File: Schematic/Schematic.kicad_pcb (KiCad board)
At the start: 2 copper layers, 1 part, among them U1 STM32F091RCT6

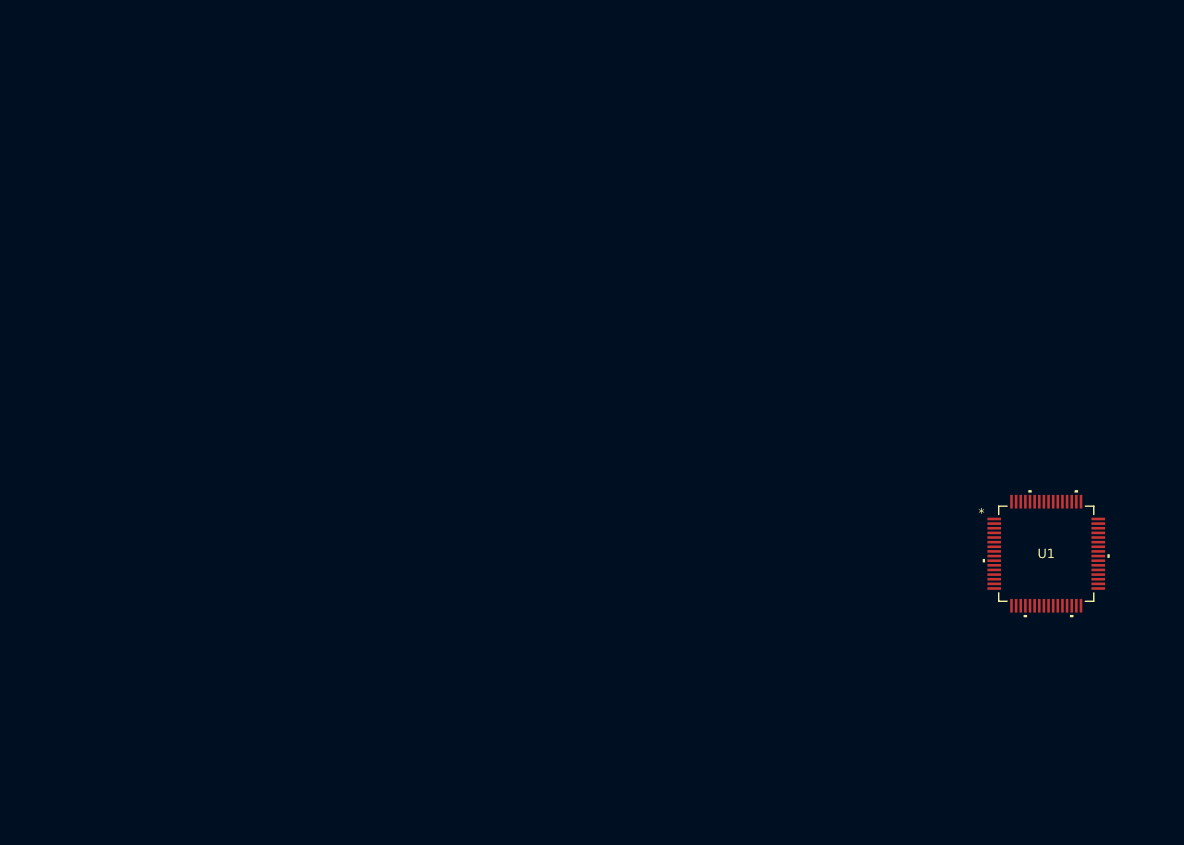
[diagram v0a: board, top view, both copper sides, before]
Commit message: Added paritial schematic including microprocessor, hub75 and keypad
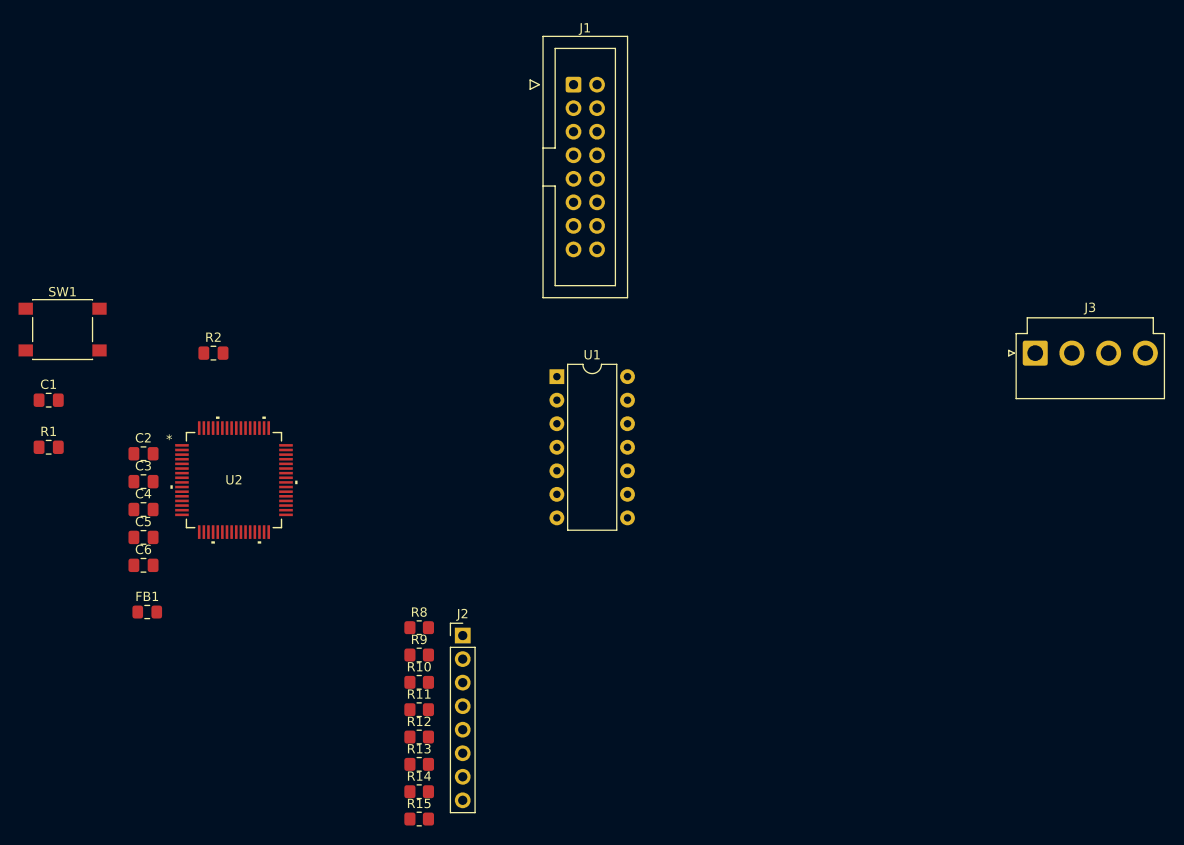
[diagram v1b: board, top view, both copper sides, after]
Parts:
- added C1: .1uF, Capacitor_SMD:C_0805_2012Metric_Pad1.18x1.45mm_HandSolder, F.Cu at (46.8, 63.5)
- added C2: .1uF, Capacitor_SMD:C_0805_2012Metric_Pad1.18x1.45mm_HandSolder, F.Cu at (57.0, 69.3)
- added C3: .1uF, Capacitor_SMD:C_0805_2012Metric_Pad1.18x1.45mm_HandSolder, F.Cu at (57.0, 72.3)
- added C4: .1uF, Capacitor_SMD:C_0805_2012Metric_Pad1.18x1.45mm_HandSolder, F.Cu at (57.0, 75.3)
- added C5: .1uF, Capacitor_SMD:C_0805_2012Metric_Pad1.18x1.45mm_HandSolder, F.Cu at (57.0, 78.3)
- added C6: .1uF, Capacitor_SMD:C_0805_2012Metric_Pad1.18x1.45mm_HandSolder, F.Cu at (57.0, 81.3)
- added FB1: Ferrite Bead, Inductor_SMD:L_0805_2012Metric_Pad1.15x1.40mm_HandSolder, F.Cu at (57.4, 86.4)
- added J1: Conn_02x08_Odd_Even, Connector_IDC:IDC-Header_2x08_P2.54mm_Vertical, F.Cu at (103.4, 29.4)
- added J2: Conn_01x08, Connector_PinHeader_2.54mm:PinHeader_1x08_P2.54mm_Vertical, F.Cu at (91.4, 88.9)
- added J3: Conn_01x04_Pin, Connector_JST:JST_VH_B4P-VH-B_1x04_P3.96mm_Vertical, F.Cu at (153.2, 58.4)
- added R1: 100K, Capacitor_SMD:C_0805_2012Metric_Pad1.18x1.45mm_HandSolder, F.Cu at (46.8, 68.6)
- added R10: 1k, Resistor_SMD:R_0805_2012Metric_Pad1.20x1.40mm_HandSolder, F.Cu at (86.7, 94.0)
- added R11: 1k, Resistor_SMD:R_0805_2012Metric_Pad1.20x1.40mm_HandSolder, F.Cu at (86.7, 96.9)
- added R12: 1k, Resistor_SMD:R_0805_2012Metric_Pad1.20x1.40mm_HandSolder, F.Cu at (86.7, 99.8)
- added R13: 1k, Resistor_SMD:R_0805_2012Metric_Pad1.20x1.40mm_HandSolder, F.Cu at (86.7, 102.8)
- added R14: 1k, Resistor_SMD:R_0805_2012Metric_Pad1.20x1.40mm_HandSolder, F.Cu at (86.7, 105.8)
- added R15: 1k, Resistor_SMD:R_0805_2012Metric_Pad1.20x1.40mm_HandSolder, F.Cu at (86.7, 108.7)
- added R2: 100K, Capacitor_SMD:C_0805_2012Metric_Pad1.18x1.45mm_HandSolder, F.Cu at (64.5, 58.4)
- added R8: 1k, Resistor_SMD:R_0805_2012Metric_Pad1.20x1.40mm_HandSolder, F.Cu at (86.7, 88.0)
- added R9: 1k, Resistor_SMD:R_0805_2012Metric_Pad1.20x1.40mm_HandSolder, F.Cu at (86.7, 91.0)
- added SW1: SW_Push, Button_Switch_SMD:SW_SPST_PTS645, F.Cu at (48.3, 55.9)
- added U2: STM32F091RCT6, STM32F091RCT6:LQFP64-10x10mm_STM, F.Cu at (66.8, 72.1)
- U1: value STM32F091RCT6 -> 74LS08; footprint STM32F091RCT6:LQFP64-10x10mm_STM -> Package_DIP:DIP-14_W7.62mm
- moved U1 56.2 mm to (101.6, 61.0)
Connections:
- U1 pad 1: unconnected-(U1-VBAT-Pad1) -> PC7
- U1 pad 10: unconnected-(U1-PC2-Pad10) -> GND
- U1 pad 12: unconnected-(U1-VSSA-Pad12) -> GND
- U1 pad 13: unconnected-(U1-VDDA-Pad13) -> GND
- U1 pad 14: unconnected-(U1-PA0-Pad14) -> +3V0
- U1 pad 2: unconnected-(U1-PC13-Pad2) -> PC6
- U1 pad 3: unconnected-(U1-PC14-OSC32_IN-Pad3) -> Net-(J1-Pin_13)
- U1 pad 4: unconnected-(U1-PC15-OSC32_OUT-Pad4) -> GND
- U1 pad 5: unconnected-(U1-PF0-OSC_IN-Pad5) -> GND
- U1 pad 7: unconnected-(U1-NRST-Pad7) -> GND
- U1 pad 9: unconnected-(U1-PC1-Pad9) -> GND

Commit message: initial CB design
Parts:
- added C10: 1mF, Capacitor_THT:CP_Radial_D10.0mm_P5.00mm, F.Cu at (150.1, 115.8)
- added C11: .1uF, Capacitor_SMD:C_0805_2012Metric_Pad1.18x1.45mm_HandSolder, F.Cu at (135.6, 113.3)
- added C12: .1uF, Capacitor_SMD:C_0805_2012Metric_Pad1.18x1.45mm_HandSolder, B.Cu at (62.2, 175.5)
- added C13: 100n, Capacitor_SMD:C_1206_3216Metric_Pad1.33x1.80mm_HandSolder, F.Cu at (109.2, 51.3)
- added C14: 10u, Capacitor_SMD:C_1206_3216Metric_Pad1.33x1.80mm_HandSolder, F.Cu at (109.2, 54.7)
- added C7: 10nF, Capacitor_SMD:C_1206_3216Metric_Pad1.33x1.80mm_HandSolder, F.Cu at (129.8, 130.1)
- added C8: 10uF, Capacitor_THT:CP_Radial_D4.0mm_P2.00mm, F.Cu at (129.3, 114.1)
- added C9: 33nF, Capacitor_SMD:C_1206_3216Metric_Pad1.33x1.80mm_HandSolder, F.Cu at (142.5, 125.0)
- added Cb1: 10nF, Capacitor_SMD:C_0805_2012Metric_Pad1.18x1.45mm_HandSolder, F.Cu at (236.3, 47.2)
- added Cin1: 180uF, Capacitor_SMD:CP_Elec_8x6.9, F.Cu at (218.3, 42.9)
- added Cinx1: 100nF, Capacitor_SMD:C_0805_2012Metric_Pad1.18x1.45mm_HandSolder, F.Cu at (236.3, 50.3)
- added Cout1: 330uF, Capacitor_SMD:CP_Elec_8x6.9, F.Cu at (218.3, 52.8)
- added D2: 550mV 5A, Diode_SMD:D_SMC-RM10_Universal_Handsoldering, F.Cu at (232.1, 41.9)
- added J4: Conn_02x01, Connector_PinHeader_2.54mm:PinHeader_2x01_P2.54mm_Vertical, F.Cu at (163.3, 115.8)
- added J5: Conn_02x05_Odd_Even, Connector_IDC:IDC-Header_2x05_P2.54mm_Vertical, F.Cu at (99.1, 103.6)
- added J6: Conn_01x03_Pin, Connector_PinHeader_2.54mm:PinHeader_1x03_P2.54mm_Vertical, F.Cu at (227.0, 48.1)
- added J7: Conn_01x02_Pin, Connector_PinHeader_2.54mm:PinHeader_1x02_P2.54mm_Vertical, F.Cu at (231.6, 48.1)
- added L1: 10uH, LIB_MSS1210-103MEB:INDPM120120X1020N, F.Cu at (219.4, 64.6)
- added LD1: LED_Red, LED_THT:LED_D5.0mm, F.Cu at (96.5, 94.0)
- added LD2: LED_Green, LED_THT:LED_D5.0mm, F.Cu at (81.0, 174.0)
- added R16: 1k, Resistor_SMD:R_1206_3216Metric_Pad1.30x1.75mm_HandSolder, F.Cu at (122.4, 154.4)
- added R17: 0, Resistor_SMD:R_1206_3216Metric_Pad1.30x1.75mm_HandSolder, F.Cu at (122.4, 159.5)
- added R18: 1k, Resistor_SMD:R_1206_3216Metric_Pad1.30x1.75mm_HandSolder, F.Cu at (122.4, 164.6)
- added R19: 0, Resistor_SMD:R_1206_3216Metric_Pad1.30x1.75mm_HandSolder, F.Cu at (122.4, 169.7)
- added R20: 1k, Resistor_SMD:R_1206_3216Metric_Pad1.30x1.75mm_HandSolder, F.Cu at (122.4, 174.8)
- added R21: 1k, Resistor_SMD:R_1206_3216Metric_Pad1.30x1.75mm_HandSolder, F.Cu at (122.4, 179.8)
- added R22: 1k, Resistor_SMD:R_1206_3216Metric_Pad1.30x1.75mm_HandSolder, F.Cu at (122.4, 184.9)
- added R23: 0, Resistor_SMD:R_1206_3216Metric_Pad1.30x1.75mm_HandSolder, F.Cu at (122.4, 190.0)
- added R24: 1k, Resistor_SMD:R_1206_3216Metric_Pad1.30x1.75mm_HandSolder, F.Cu at (90.7, 153.9)
- added R25: 1k, Resistor_SMD:R_1206_3216Metric_Pad1.30x1.75mm_HandSolder, F.Cu at (90.9, 159.3)
- added R26: 1k, Resistor_SMD:R_1206_3216Metric_Pad1.30x1.75mm_HandSolder, F.Cu at (90.9, 164.3)
- added R27: 1k, Resistor_SMD:R_1206_3216Metric_Pad1.30x1.75mm_HandSolder, F.Cu at (90.9, 169.4)
- added R28: 1k, Resistor_SMD:R_1206_3216Metric_Pad1.30x1.75mm_HandSolder, F.Cu at (91.2, 174.5)
- added R29: 1k, Resistor_SMD:R_1206_3216Metric_Pad1.30x1.75mm_HandSolder, F.Cu at (91.2, 179.6)
- added R3: 3.2k, Resistor_SMD:R_1206_3216Metric_Pad1.30x1.75mm_HandSolder, F.Cu at (129.8, 135.1)
- added R30: 1k, Resistor_SMD:R_1206_3216Metric_Pad1.30x1.75mm_HandSolder, F.Cu at (90.7, 184.7)
- added R31: 1k, Resistor_SMD:R_1206_3216Metric_Pad1.30x1.75mm_HandSolder, F.Cu at (91.2, 189.7)
- added R32: 1k, Resistor_SMD:R_1206_3216Metric_Pad1.30x1.75mm_HandSolder, B.Cu at (72.6, 190.2)
- added R33: 1k, Resistor_SMD:R_1206_3216Metric_Pad1.30x1.75mm_HandSolder, B.Cu at (72.6, 185.2)
- added R34: 1k, Resistor_SMD:R_1206_3216Metric_Pad1.30x1.75mm_HandSolder, F.Cu at (72.6, 179.8)
- added R35: 1k, Resistor_SMD:R_1206_3216Metric_Pad1.30x1.75mm_HandSolder, F.Cu at (72.6, 174.8)
- added R36: 1k, Resistor_SMD:R_1206_3216Metric_Pad1.30x1.75mm_HandSolder, F.Cu at (48.8, 175.0)
- added R37: 1k, Resistor_SMD:R_1206_3216Metric_Pad1.30x1.75mm_HandSolder, F.Cu at (48.8, 180.1)
- added R38: 1k, Resistor_SMD:R_1206_3216Metric_Pad1.30x1.75mm_HandSolder, F.Cu at (48.8, 185.2)
- added R39: 1k, Resistor_SMD:R_1206_3216Metric_Pad1.30x1.75mm_HandSolder, F.Cu at (48.8, 190.2)
- added R4: 10, Resistor_SMD:R_1206_3216Metric_Pad1.30x1.75mm_HandSolder, F.Cu at (142.5, 117.4)
- added R40: 5.1k, Resistor_SMD:R_1206_3216Metric_Pad1.30x1.75mm_HandSolder, F.Cu at (81.5, 179.4)
- added R5: 20k, Resistor_SMD:R_1206_3216Metric_Pad1.30x1.75mm_HandSolder, F.Cu at (136.4, 135.1)
- added R6: 5.1k, Resistor_SMD:R_1206_3216Metric_Pad1.30x1.75mm_HandSolder, F.Cu at (88.4, 94.7)
- added R7: 0, Resistor_SMD:R_1206_3216Metric_Pad1.30x1.75mm_HandSolder, F.Cu at (144.8, 103.1)
- added U3: LM386, Package_DIP:DIP-8_W7.62mm, F.Cu at (126.7, 125.7)
- added U4: LM2678S-12, LM2678-TO263:TS7B, F.Cu at (232.9, 63.9)
- added U5: LD1117S33TR_SOT223, Package_TO_SOT_THT:TO-220-3_Vertical, F.Cu at (118.6, 57.4)
- C1, C2, C3, C4, C5, C6, FB1, R1, R2: moved to B.Cu
- R10, R11, R12, R13, R14, R15, R8, R9: footprint Resistor_SMD:R_0805_2012Metric_Pad1.20x1.40mm_HandSolder -> Resistor_SMD:R_1206_3216Metric_Pad1.30x1.75mm_HandSolder
- moved U1 133.8 mm to (65.3, 189.7), turned to 180 degrees
- moved J1 132.9 mm to (105.4, 162.3)
- moved C1 104.3 mm to (117.1, 140.5), turned to 45 degrees
- moved R1 100.8 mm to (113.8, 143.8), turned to 45 degrees
- moved R2 92.6 mm to (100.6, 143.8), turned to -45 degrees
- moved SW1 89.8 mm to (125.7, 101.3)
- moved C3 85.0 mm to (105.9, 141.8), turned to -90 degrees
- moved C4 78.9 mm to (112.0, 131.8), turned to -45 degrees
- moved C6 77.5 mm to (112.3, 135.6), turned to -135 degrees
- moved C2 75.9 mm to (99.3, 132.3), turned to 45 degrees
- moved U2 73.0 mm to (106.0, 133.7), turned to 135 degrees
- moved FB1 70.3 mm to (109.5, 133.6), turned to -135 degrees
- moved C5 70.1 mm to (107.4, 127.0), turned to -45 degrees
- moved R15 41.7 mm to (76.5, 149.1), turned to 180 degrees
- moved J2 40.0 mm to (67.8, 121.2)
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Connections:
- net /microprocessor/3VA renamed VA
- C6 pad 2: GND -> GNDA
- J1 pad 1: PC0 -> Net-(J1-Pin_1)
- J1 pad 10: PC9 -> Net-(J1-Pin_10)
- J1 pad 11: PC10 -> Net-(J1-Pin_11)
- J1 pad 12: PC11 -> Net-(J1-Pin_12)
- J1 pad 14: PC12 -> Net-(J1-Pin_14)
- J1 pad 15: PC13 -> Net-(J1-Pin_15)
- J1 pad 16: GND -> Net-(J1-Pin_16)
- J1 pad 2: PC1 -> Net-(J1-Pin_2)
- J1 pad 3: PC2 -> Net-(J1-Pin_3)
- J1 pad 4: GND -> Net-(J1-Pin_4)
- J1 pad 5: PC3 -> Net-(J1-Pin_5)
- J1 pad 6: PC4 -> Net-(J1-Pin_6)
- J1 pad 7: PC5 -> Net-(J1-Pin_7)
- J1 pad 8: GND -> Net-(J1-Pin_8)
- J1 pad 9: PC8 -> Net-(J1-Pin_9)
- R15 pad 1: unconnected-(R15-Pad1) -> PB7
- U1 pad 1: PC7 -> Net-(R32-Pad2)
- U1 pad 10: GND -> Net-(R37-Pad2)
- U1 pad 12: GND -> Net-(R38-Pad2)
- U1 pad 13: GND -> Net-(R39-Pad2)
- U1 pad 2: PC6 -> Net-(R33-Pad2)
- U1 pad 3: Net-(J1-Pin_13) -> Net-(R30-Pad2)
- U1 pad 4: GND -> Net-(R34-Pad2)
- U1 pad 5: GND -> Net-(R35-Pad2)
- U1 pad 9: GND -> Net-(R36-Pad2)
- U2 pad 12: GND -> GNDA
- U2 pad 20: unconnected-(U2-PA4-Pad20) -> PA4
- U2 pad 3: PC14 -> /microprocessor/SWDIO_IN
- U2 pad 4: PC15 -> /microprocessor/SWCLK_IN
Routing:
- net PC7: track 0.00 -> 82.1 mm, vias 0 -> 1
- net PC6: track 0.00 -> 78.8 mm, vias 0 -> 1
- net /microprocessor/NRST: track 0.00 -> 76.0 mm, vias 0 -> 2
- net VA: track 0.00 -> 75.2 mm, vias 0 -> 1
- net PC12: track 0.00 -> 63.8 mm, vias 0 -> 2
- net +3V0: track 0.00 -> 62.8 mm, vias 0 -> 5
- net PC11: track 0.00 -> 60.1 mm, vias 0 -> 2
- net PC13: track 0.00 -> 59.5 mm, vias 0 -> 2
- net PC8: track 0.00 -> 58.2 mm, vias 0 -> 2
- net PC9: track 0.00 -> 57.0 mm, vias 0 -> 2
- net PC10: track 0.00 -> 54.3 mm, vias 0 -> 2
- net PC5: track 0.00 -> 52.6 mm, vias 0 -> 2
- net PB2: track 0.00 -> 46.6 mm
- net PB1: track 0.00 -> 43.3 mm
- net PC4: track 0.00 -> 43.1 mm, vias 0 -> 2
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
